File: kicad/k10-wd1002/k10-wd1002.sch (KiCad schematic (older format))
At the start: 6 parts, among them J1 Kaypro, J2 WD1002, U1 74LS00, U2 74LS138

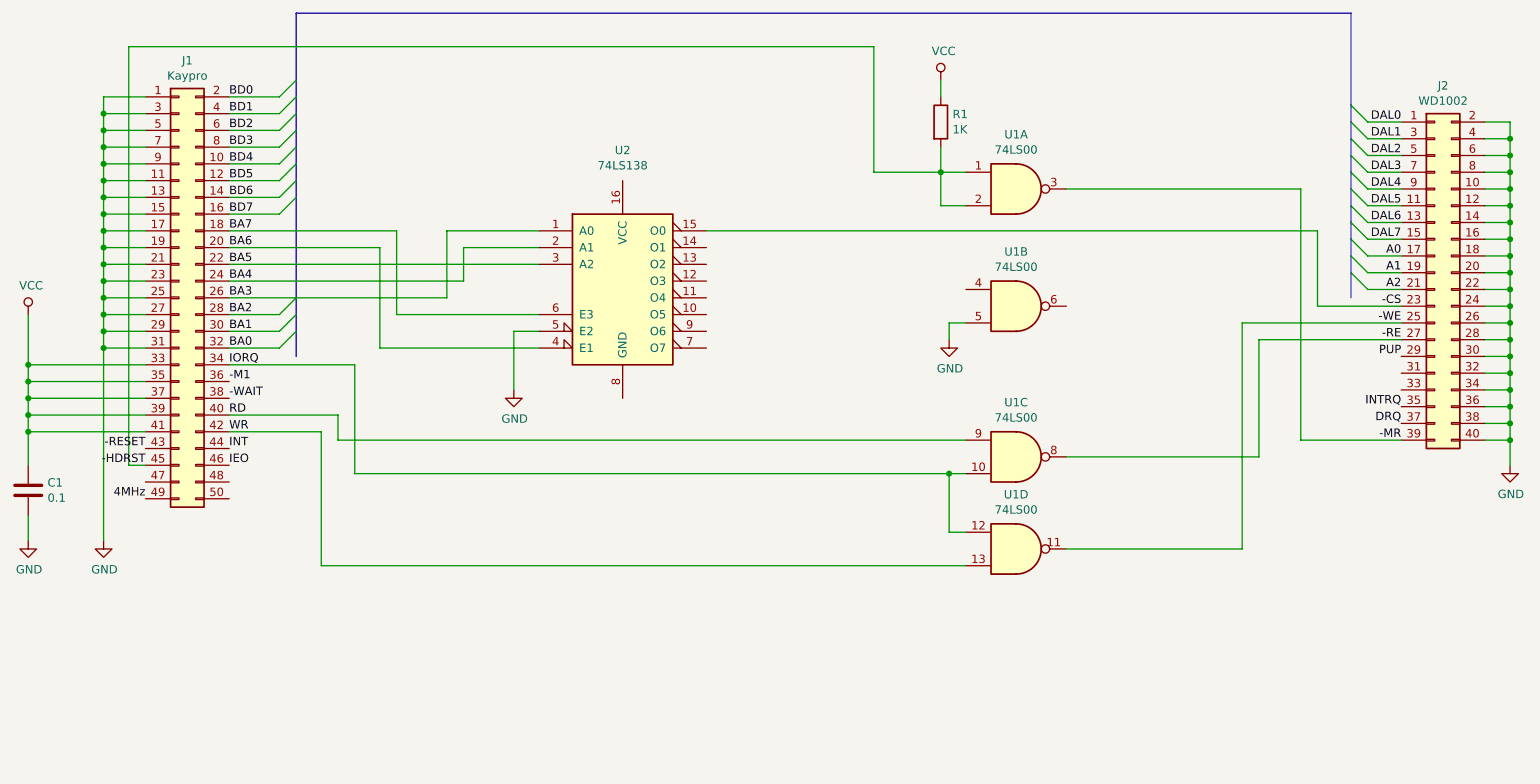
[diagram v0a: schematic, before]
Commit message: Revise and correct K10-WD1002 schematic
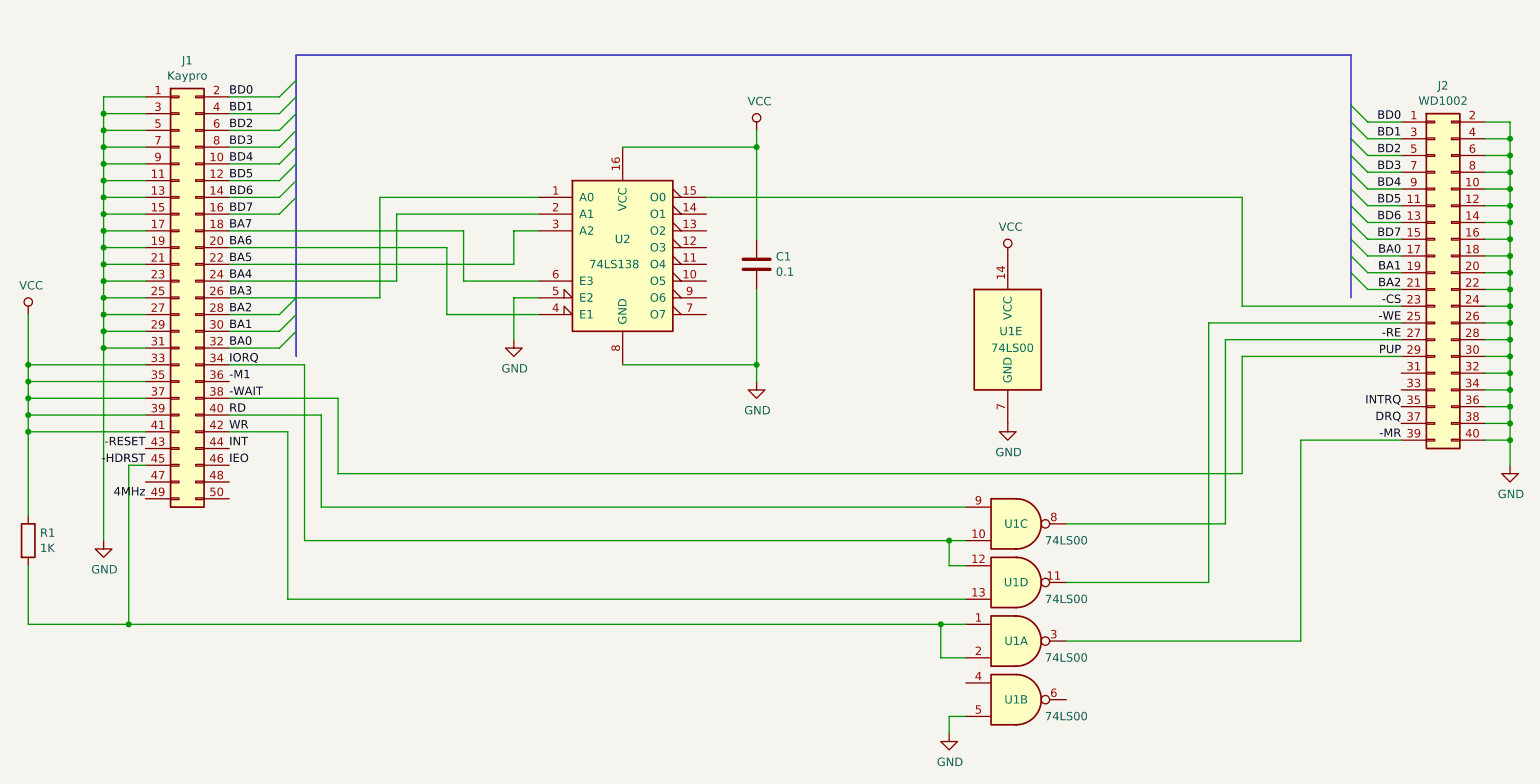
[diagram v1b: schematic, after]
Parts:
- added unit 5 of U1
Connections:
- net A0 is gone; now on net BA0: J2.17 (Pin_17)
- net A1 is gone; now on net BA1: J2.19 (Pin_19)
- net A2 is gone; now on net BA2: J2.21 (Pin_21)
- net DAL0 is gone; now on net BD0: J2.1 (Pin_1)
- net DAL1 is gone; now on net BD1: J2.3 (Pin_3)
- net DAL2 is gone; now on net BD2: J2.5 (Pin_5)
- net DAL3 is gone; now on net BD3: J2.7 (Pin_7)
- net DAL4 is gone; now on net BD4: J2.9 (Pin_9)
- net DAL5 is gone; now on net BD5: J2.11 (Pin_11)
- net DAL6 is gone; now on net BD6: J2.13 (Pin_13)
- net DAL7 is gone; now on net BD7: J2.15 (Pin_15)
- net PUP is gone; now on net -WAIT: J2.29 (Pin_29)
- net GND: now also U2.8 (GND), U1.7 (GND)
- net VCC: now also U2.16 (VCC), U1.14 (VCC)
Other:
- moved on the sheet: C1, R1, U1A, U1B, U1C, U1D, U2

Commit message: Finish PCB layout
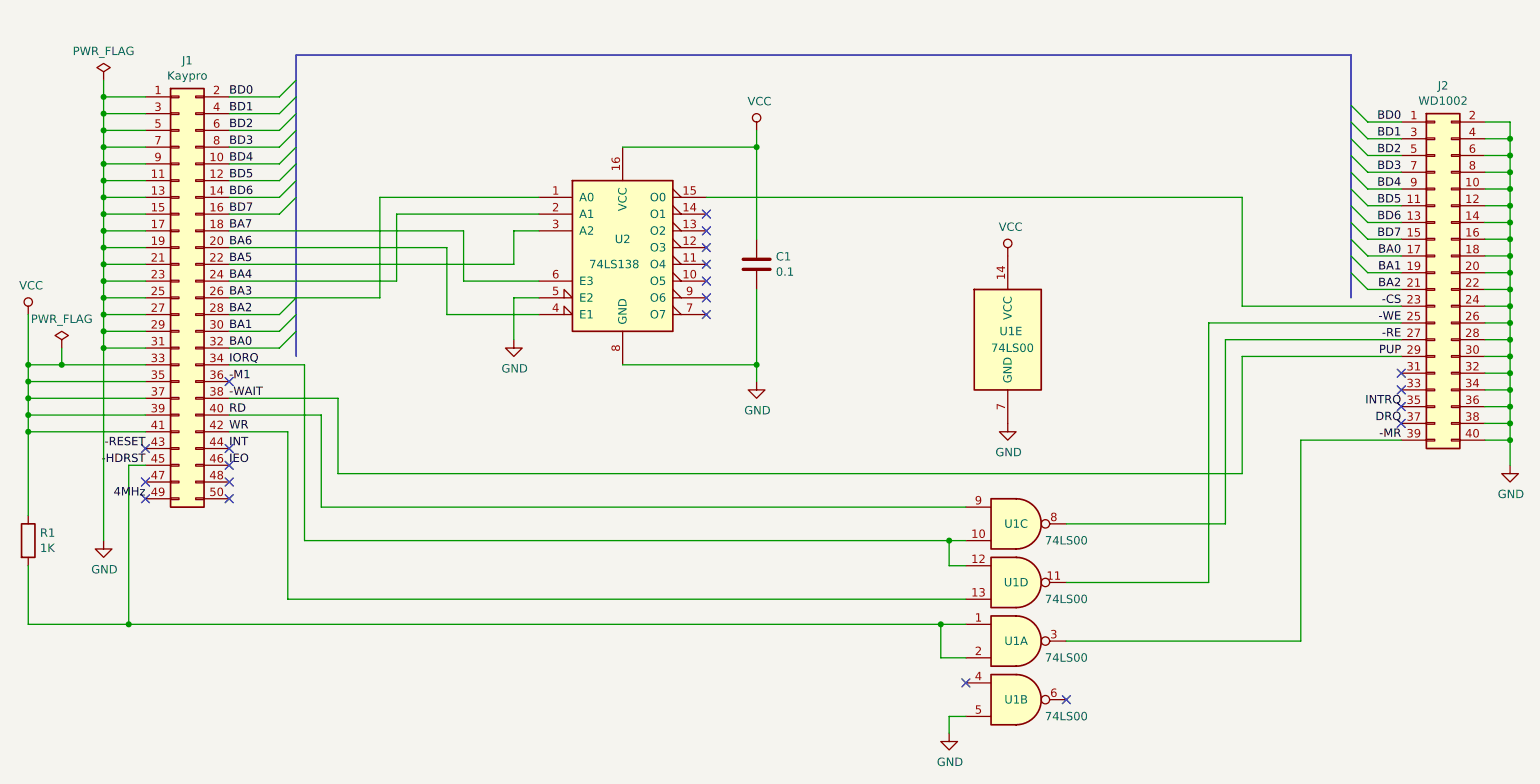
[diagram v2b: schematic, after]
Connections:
- no-connect marks 0 -> 21
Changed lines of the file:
@@
 $EndComp
 $Comp
-L power:GND #PWR?
+L power:GND #PWR0101
 U 1 1 6233AAB4
 P 1800 4800
-F 0 "#PWR?" H 1800 4550 50  0001 C CNN
+F 0 "#PWR0101" H 1800 4550 50  0001 C CNN
 F 1 "GND" H 1805 4627 50  0000 C CNN
 F 2 "" H 1800 4800 50  0001 C CNN
@@
 	1800 3550 1800 3450
 $Comp
-L power:VCC #PWR?
+L power:VCC #PWR0102
 U 1 1 6233E191
 P 1350 3450
-F 0 "#PWR?" H 1350 3300 50  0001 C CNN
+F 0 "#PWR0102" H 1350 3300 50  0001 C CNN
 F 1 "VCC" H 1367 3623 50  0000 C CNN
 F 2 "" H 1350 3450 50  0001 C CNN
@@
 	1350 3850 1350 3950
 Wire Wire Line
-	2050 3750 1350 3750
+	2050 3750 1550 3750
 Connection ~ 1350 3750
 Wire Wire Line
@@
 $EndComp
 $Comp
-L power:GND #PWR?
+L power:GND #PWR0103
 U 1 1 623631FC
 P 5700 3850
-F 0 "#PWR?" H 5700 3600 50  0001 C CNN
+F 0 "#PWR0103" H 5700 3600 50  0001 C CNN
 F 1 "GND" H 5705 3677 50  0000 C CNN
 F 2 "" H 5700 3850 50  0001 C CNN
@@
 	6850 4800 6950 4800
 $Comp
-L power:GND #PWR?
+L power:GND #PWR0104
 U 1 1 623723A4
 P 10200 4350
-F 0 "#PWR?" H 10200 4100 50  0001 C CNN
+F 0 "#PWR0104" H 10200 4100 50  0001 C CNN
 F 1 "GND" H 10205 4177 50  0000 C CNN
 F 2 "" H 10200 4350 50  0001 C CNN
@@
 	8600 3400 9550 3400
 $Comp
-L power:GND #PWR?
+L power:GND #PWR0105
 U 1 1 623A9BEF
 P 6850 5950
-F 0 "#PWR?" H 6850 5700 50  0001 C CNN
+F 0 "#PWR0105" H 6850 5700 50  0001 C CNN
 F 1 "GND" H 6855 5777 50  0000 C CNN
 F 2 "" H 6850 5950 50  0001 C CNN
@@
 	3550 2850 4400 2850
 $Comp
-L power:GND #PWR?
+L power:GND #PWR0106
 U 1 1 623B8315
 P 4250 3600
-F 0 "#PWR?" H 4250 3350 50  0001 C CNN
+F 0 "#PWR0106" H 4250 3350 50  0001 C CNN
 F 1 "GND" H 4255 3427 50  0000 C CNN
 F 2 "" H 4250 3600 50  0001 C CNN
@@
 $EndComp
 $Comp
-L power:VCC #PWR?
+L power:VCC #PWR0107
 U 1 1 623792D9
 P 5700 2350
-F 0 "#PWR?" H 5700 2200 50  0001 C CNN
+F 0 "#PWR0107" H 5700 2200 50  0001 C CNN
 F 1 "VCC" H 5717 2523 50  0000 C CNN
 F 2 "" H 5700 2350 50  0001 C CNN
@@
 $EndComp
 $Comp
-L power:VCC #PWR?
+L power:VCC #PWR0108
 U 1 1 62379B56
 P 7200 3100
-F 0 "#PWR?" H 7200 2950 50  0001 C CNN
+F 0 "#PWR0108" H 7200 2950 50  0001 C CNN
 F 1 "VCC" H 7217 3273 50  0000 C CNN
 F 2 "" H 7200 3100 50  0001 C CNN
@@
 $EndComp
 $Comp
-L power:GND #PWR?
+L power:GND #PWR0109
 U 1 1 6237A952
 P 7200 4100
-F 0 "#PWR?" H 7200 3850 50  0001 C CNN
+F 0 "#PWR0109" H 7200 3850 50  0001 C CNN
 F 1 "GND" H 7205 3927 50  0000 C CNN
 F 2 "" H 7200 4100 50  0001 C CNN
@@
 Wire Wire Line
 	8600 3700 9550 3700
+NoConn ~ 2550 3850
+NoConn ~ 2550 4250
+NoConn ~ 2550 4350
+NoConn ~ 2550 4450
+NoConn ~ 2550 4550
+NoConn ~ 2050 4550
+NoConn ~ 2050 4450
+NoConn ~ 2050 4250
+NoConn ~ 6950 5650
+NoConn ~ 9550 3800
+NoConn ~ 9550 3900
+NoConn ~ 9550 4000
+NoConn ~ 9550 4100
+NoConn ~ 7550 5750
+NoConn ~ 5400 2850
+NoConn ~ 5400 2950
+NoConn ~ 5400 3050
+NoConn ~ 5400 3150
+NoConn ~ 5400 3250
+NoConn ~ 5400 3350
+NoConn ~ 5400 3450
+$Comp
+L power:PWR_FLAG #FLG0101
+U 1 1 62400F09
+P 1550 3650
+F 0 "#FLG0101" H 1550 3725 50  0001 C CNN
+F 1 "PWR_FLAG" H 1550 3823 50  0000 C CNN
+F 2 "" H 1550 3650 50  0001 C CNN
+F 3 "~" H 1550 3650 50  0001 C CNN
+	1    1550 3650
+	1    0    0    -1
+$EndComp
+$Comp
+L power:PWR_FLAG #FLG0102
+U 1 1 62401B5A
+P 1800 2050
+F 0 "#FLG0102" H 1800 2125 50  0001 C CNN
+F 1 "PWR_FLAG" H 1800 2223 50  0000 C CNN
+F 2 "" H 1800 2050 50  0001 C CNN
+F 3 "~" H 1800 2050 50  0001 C CNN
+	1    1800 2050
+	1    0    0    -1
+$EndComp
+Wire Wire Line
+	1550 3650 1550 3750
+Connection ~ 1550 3750
+Wire Wire Line
+	1550 3750 1350 3750
+Wire Wire Line
+	1800 2050 1800 2150
 Wire Wire Line
 	2550 3350 3450 3350
@@
 Wire Bus Line
 	9250 1900 9250 3350
+Connection ~ 1800 2150
 $EndSCHEMATC
